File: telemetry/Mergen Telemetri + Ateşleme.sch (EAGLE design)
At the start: 78 parts, among them J2 U.FL, Q2 IRLML6344TRPBF, Q3 IRLML6344TRPBF, U1 STM32F401CCU6UFQFPN-48_7X7X0P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, U2 ADXL345BCCZ, U3 LPS22HB, U4 L86, U6 AMS1117-3.3, U7 AMS1117-3.3, Y1 ABM3B-26.000MHZ-10-1-U-T

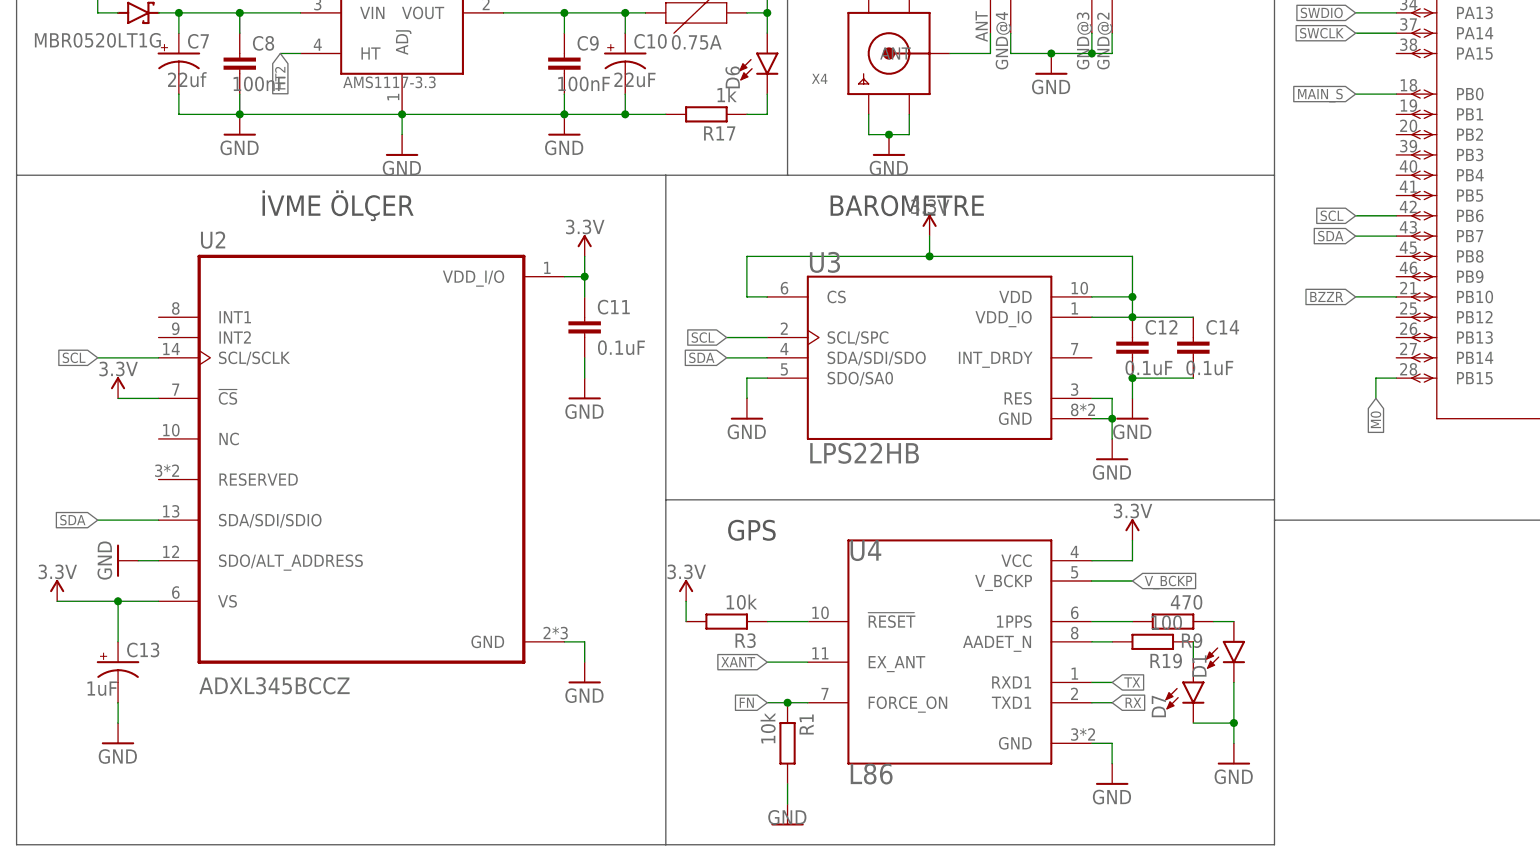
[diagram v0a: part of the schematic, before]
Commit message: Some modification was maken on the LPS22HB and ADXL345
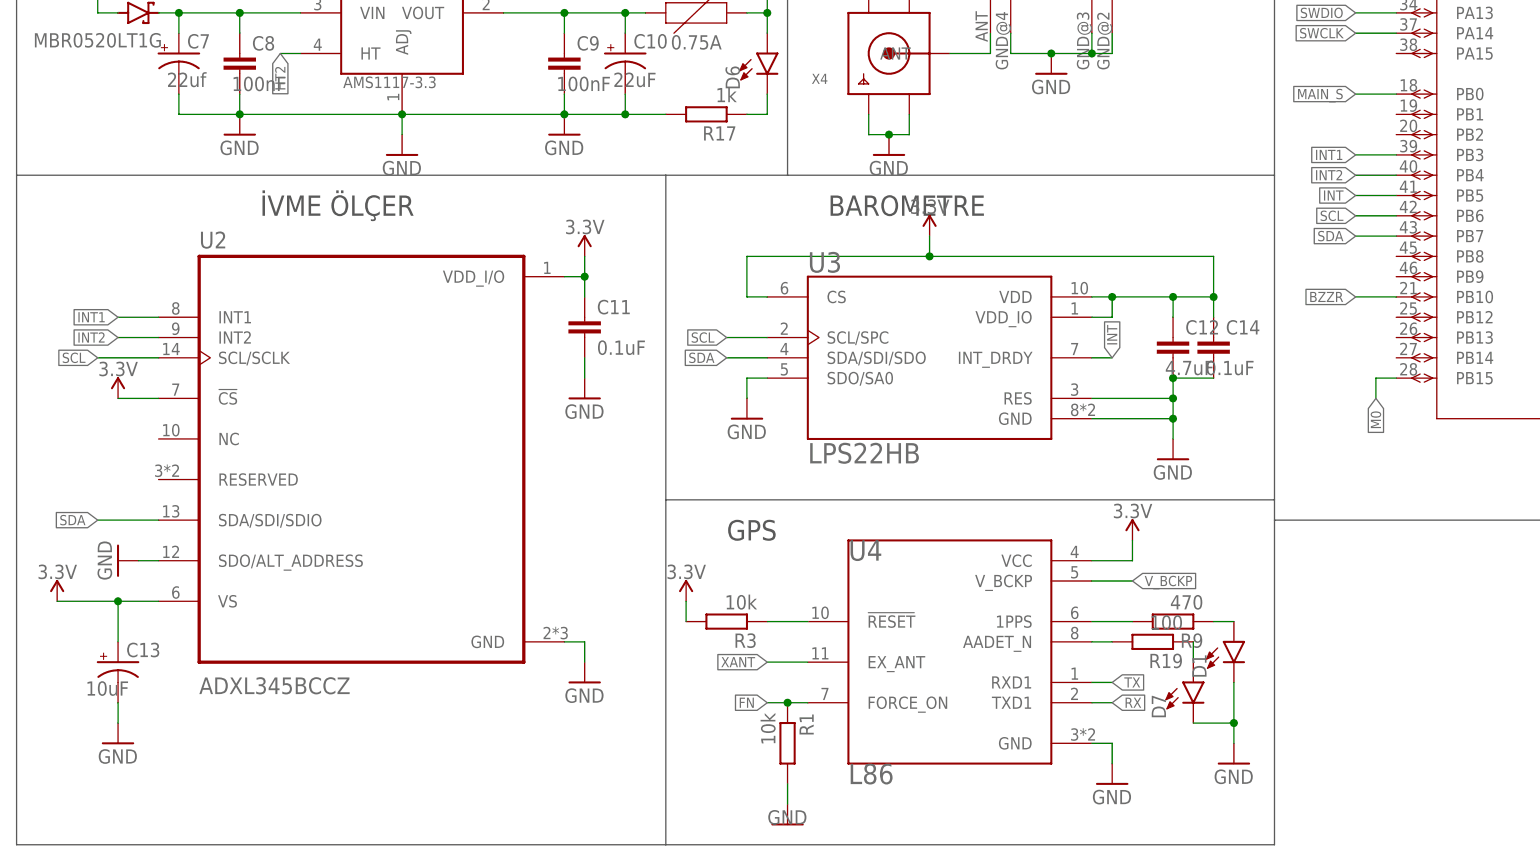
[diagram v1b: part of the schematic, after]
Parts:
- C12: value 0.1uF -> 4.7uF
- C13: value 1uF -> 10uF
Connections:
- new net INT: U1A.PB5, U3.INT_DRDY
- new net INT1: U1A.PB3, U2.INT1
- new net INT2: U1A.PB4, U2.INT2
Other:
- moved on the sheet: C12, C14
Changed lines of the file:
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@@
 <part name="GND7" library="supply1" library_urn="urn:adsk.eagle:library:371" deviceset="GND" device=""/>
 <part name="GND8" library="supply1" library_urn="urn:adsk.eagle:library:371" deviceset="GND" device=""/>
-<part name="C13" library="rcl" library_urn="urn:adsk.eagle:library:334" deviceset="CPOL-US" device="R/2012-12W" package3d_urn="urn:adsk.eagle:package:23419/2" value="1uF"/>
+<part name="C13" library="rcl" library_urn="urn:adsk.eagle:library:334" deviceset="CPOL-US" device="R/2012-12W" package3d_urn="urn:adsk.eagle:package:23419/2" value="10uF"/>
 <part name="GND9" library="supply1" library_urn="urn:adsk.eagle:library:371" deviceset="GND" device=""/>
-<part name="GND10" library="supply1" library_urn="urn:adsk.eagle:library:371" deviceset="GND" device=""/>
-<part name="C12" library="rcl" library_urn="urn:adsk.eagle:library:334" deviceset="C-EU" device="C0402K" package3d_urn="urn:adsk.eagle:package:23679/2" value="0.1uF"/>
+<part name="C12" library="rcl" library_urn="urn:adsk.eagle:library:334" deviceset="C-EU" device="C0402K" package3d_urn="urn:adsk.eagle:package:23679/2" value="4.7uF"/>
 <part name="C14" library="rcl" library_urn="urn:adsk.eagle:library:334" deviceset="C-EU" device="C0402K" package3d_urn="urn:adsk.eagle:package:23679/2" value="0.1uF"/>
 <part name="GND11" library="supply1" library_urn="urn:adsk.eagle:library:371" deviceset="GND" device=""/>
@@
 <attribute name="VALUE" x="-157.48" y="-83.82" size="1.778" layer="96"/>
 </instance>
-<instance part="GND10" gate="1" x="-30.48" y="-45.72" smashed="yes">
-<attribute name="VALUE" x="-33.02" y="-48.26" size="1.778" layer="96"/>
-</instance>
-<instance part="C12" gate="G$1" x="-27.94" y="-30.48" smashed="yes">
-<attribute name="NAME" x="-26.416" y="-30.099" size="1.778" layer="95"/>
-<attribute name="VALUE" x="-28.956" y="-35.179" size="1.778" layer="96"/>
-</instance>
-<instance part="C14" gate="G$1" x="-20.32" y="-30.48" smashed="yes">
-<attribute name="NAME" x="-18.796" y="-30.099" size="1.778" layer="95"/>
-<attribute name="VALUE" x="-21.336" y="-35.179" size="1.778" layer="96"/>
-</instance>
-<instance part="GND11" gate="1" x="-27.94" y="-40.64" smashed="yes">
-<attribute name="VALUE" x="-30.48" y="-43.18" size="1.778" layer="96"/>
+<instance part="C12" gate="G$1" x="-22.86" y="-30.48" smashed="yes">
+<attribute name="NAME" x="-21.336" y="-30.099" size="1.778" layer="95"/>
+<attribute name="VALUE" x="-23.876" y="-35.179" size="1.778" layer="96"/>
+</instance>
+<instance part="C14" gate="G$1" x="-17.78" y="-30.48" smashed="yes">
+<attribute name="NAME" x="-16.256" y="-30.099" size="1.778" layer="95"/>
+<attribute name="VALUE" x="-18.796" y="-35.179" size="1.778" layer="96"/>
+</instance>
+<instance part="GND11" gate="1" x="-22.86" y="-45.72" smashed="yes">
+<attribute name="VALUE" x="-25.4" y="-48.26" size="1.778" layer="96"/>
 </instance>
 <instance part="GND12" gate="1" x="-76.2" y="-40.64" smashed="yes">
@@
 </segment>
 <segment>
+<pinref part="C12" gate="G$1" pin="2"/>
+<wire x1="-22.86" y1="-35.56" x2="-17.78" y2="-35.56" width="0.1524" layer="91"/>
+<pinref part="C14" gate="G$1" pin="2"/>
+<wire x1="-22.86" y1="-35.56" x2="-22.86" y2="-38.1" width="0.1524" layer="91"/>
+<junction x="-22.86" y="-35.56"/>
+<pinref part="GND11" gate="1" pin="GND"/>
+<pinref part="U3" gate="G$1" pin="RES"/>
+<wire x1="-22.86" y1="-38.1" x2="-22.86" y2="-40.64" width="0.1524" layer="91"/>
+<wire x1="-22.86" y1="-40.64" x2="-22.86" y2="-43.18" width="0.1524" layer="91"/>
+<wire x1="-33.02" y1="-38.1" x2="-22.86" y2="-38.1" width="0.1524" layer="91"/>
+<junction x="-22.86" y="-38.1"/>
 <pinref part="U3" gate="G$1" pin="GND"/>
-<wire x1="-33.02" y1="-40.64" x2="-30.48" y2="-40.64" width="0.1524" layer="91"/>
-<wire x1="-30.48" y1="-40.64" x2="-30.48" y2="-43.18" width="0.1524" layer="91"/>
-<pinref part="GND10" gate="1" pin="GND"/>
-<wire x1="-30.48" y1="-40.64" x2="-30.48" y2="-38.1" width="0.1524" layer="91"/>
-<junction x="-30.48" y="-40.64"/>
-<pinref part="U3" gate="G$1" pin="RES"/>
-<wire x1="-30.48" y1="-38.1" x2="-33.02" y2="-38.1" width="0.1524" layer="91"/>
-</segment>
-<segment>
-<pinref part="C12" gate="G$1" pin="2"/>
-<wire x1="-27.94" y1="-35.56" x2="-20.32" y2="-35.56" width="0.1524" layer="91"/>
-<pinref part="C14" gate="G$1" pin="2"/>
-<wire x1="-27.94" y1="-35.56" x2="-27.94" y2="-38.1" width="0.1524" layer="91"/>
-<junction x="-27.94" y="-35.56"/>
-<pinref part="GND11" gate="1" pin="GND"/>
+<wire x1="-33.02" y1="-40.64" x2="-22.86" y2="-40.64" width="0.1524" layer="91"/>
+<junction x="-22.86" y="-40.64"/>
 </segment>
 <segment>
@@
 <segment>
 <pinref part="U3" gate="G$1" pin="VDD_IO"/>
-<pinref part="C12" gate="G$1" pin="1"/>
-<wire x1="-33.02" y1="-27.94" x2="-27.94" y2="-27.94" width="0.1524" layer="91"/>
-<pinref part="C14" gate="G$1" pin="1"/>
-<wire x1="-27.94" y1="-27.94" x2="-20.32" y2="-27.94" width="0.1524" layer="91"/>
-<junction x="-27.94" y="-27.94"/>
+<wire x1="-33.02" y1="-27.94" x2="-30.48" y2="-27.94" width="0.1524" layer="91"/>
 <pinref part="U3" gate="G$1" pin="VDD"/>
-<wire x1="-33.02" y1="-25.4" x2="-27.94" y2="-25.4" width="0.1524" layer="91"/>
-<wire x1="-27.94" y1="-25.4" x2="-27.94" y2="-27.94" width="0.1524" layer="91"/>
-<wire x1="-27.94" y1="-25.4" x2="-27.94" y2="-20.32" width="0.1524" layer="91"/>
-<junction x="-27.94" y="-25.4"/>
+<wire x1="-33.02" y1="-25.4" x2="-30.48" y2="-25.4" width="0.1524" layer="91"/>
+<wire x1="-30.48" y1="-25.4" x2="-22.86" y2="-25.4" width="0.1524" layer="91"/>
+<wire x1="-22.86" y1="-25.4" x2="-17.78" y2="-25.4" width="0.1524" layer="91"/>
+<wire x1="-17.78" y1="-25.4" x2="-17.78" y2="-20.32" width="0.1524" layer="91"/>
 <wire x1="-76.2" y1="-20.32" x2="-53.34" y2="-20.32" width="0.1524" layer="91"/>
 <pinref part="U3" gate="G$1" pin="CS"/>
-<wire x1="-53.34" y1="-20.32" x2="-27.94" y2="-20.32" width="0.1524" layer="91"/>
+<wire x1="-53.34" y1="-20.32" x2="-17.78" y2="-20.32" width="0.1524" layer="91"/>
 <wire x1="-73.66" y1="-25.4" x2="-76.2" y2="-25.4" width="0.1524" layer="91"/>
 <wire x1="-76.2" y1="-25.4" x2="-76.2" y2="-20.32" width="0.1524" layer="91"/>
@@
 <wire x1="-53.34" y1="-17.78" x2="-53.34" y2="-20.32" width="0.1524" layer="91"/>
 <junction x="-53.34" y="-20.32"/>
+<wire x1="-30.48" y1="-27.94" x2="-30.48" y2="-25.4" width="0.1524" layer="91"/>
+<junction x="-30.48" y="-25.4"/>
+<pinref part="C12" gate="G$1" pin="1"/>
+<wire x1="-22.86" y1="-27.94" x2="-22.86" y2="-25.4" width="0.1524" layer="91"/>
+<junction x="-22.86" y="-25.4"/>
+<pinref part="C14" gate="G$1" pin="1"/>
+<wire x1="-17.78" y1="-27.94" x2="-17.78" y2="-25.4" width="0.1524" layer="91"/>
+<junction x="-17.78" y="-25.4"/>
 </segment>
 <segment>
@@
 </segment>
 </net>
+<net name="INT1" class="0">
+<segment>
+<pinref part="U2" gate="A" pin="INT1"/>
+<wire x1="-149.86" y1="-27.94" x2="-154.94" y2="-27.94" width="0.1524" layer="91"/>
+<label x="-154.94" y="-27.94" size="1.27" layer="95" rot="R180" xref="yes"/>
+</segment>
+<segment>
+<pinref part="U1" gate="A" pin="PB3"/>
+<wire x1="5.08" y1="-7.62" x2="0" y2="-7.62" width="0.1524" layer="91"/>
+<label x="0" y="-7.62" size="1.27" layer="95" rot="R180" xref="yes"/>
+</segment>
+</net>
+<net name="INT2" class="0">
+<segment>
+<pinref part="U2" gate="A" pin="INT2"/>
+<wire x1="-149.86" y1="-30.48" x2="-154.94" y2="-30.48" width="0.1524" layer="91"/>
+<label x="-154.94" y="-30.48" size="1.27" layer="95" rot="R180" xref="yes"/>
+</segment>
+<segment>
+<pinref part="U1" gate="A" pin="PB4"/>
+<wire x1="5.08" y1="-10.16" x2="0" y2="-10.16" width="0.1524" layer="91"/>
+<label x="0" y="-10.16" size="1.27" layer="95" rot="R180" xref="yes"/>
+</segment>
+</net>
+<net name="INT" class="0">
+<segment>
+<pinref part="U3" gate="G$1" pin="INT_DRDY"/>
+<wire x1="-33.02" y1="-33.02" x2="-30.48" y2="-33.02" width="0.1524" layer="91"/>
+<label x="-30.48" y="-33.02" size="1.27" layer="95" rot="R90" xref="yes"/>
+</segment>
+<segment>
+<pinref part="U1" gate="A" pin="PB5"/>
+<wire x1="5.08" y1="-12.7" x2="0" y2="-12.7" width="0.1524" layer="91"/>
+<label x="0" y="-12.7" size="1.27" layer="95" rot="R180" xref="yes"/>
+</segment>
+</net>
